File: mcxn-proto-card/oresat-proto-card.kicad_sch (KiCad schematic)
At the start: 0 parts

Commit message: Fully routed MCXN947 proto card, still needs final polish.
Big cleanup of the proto card's OPD, bringing it up to modern standards. Also fixed the v2 backplane connector. Added the MCXN937 processor, and breakouts for the unused pins. Switched to the new debug connector, which will be fun. That's it!
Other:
- title: OreSat M0 Proto Card -> OreSat MCXN Proto Card
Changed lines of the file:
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@@
 	(paper "USLedger")
 	(title_block
-		(title "OreSat M0 Proto Card")
-		(date "2025-06-29")
-		(rev "5.0")
+		(title "OreSat MCXN Proto Card")
+		(date "2025-11-13")
+		(rev "6.0")
 	)
 	(sheet

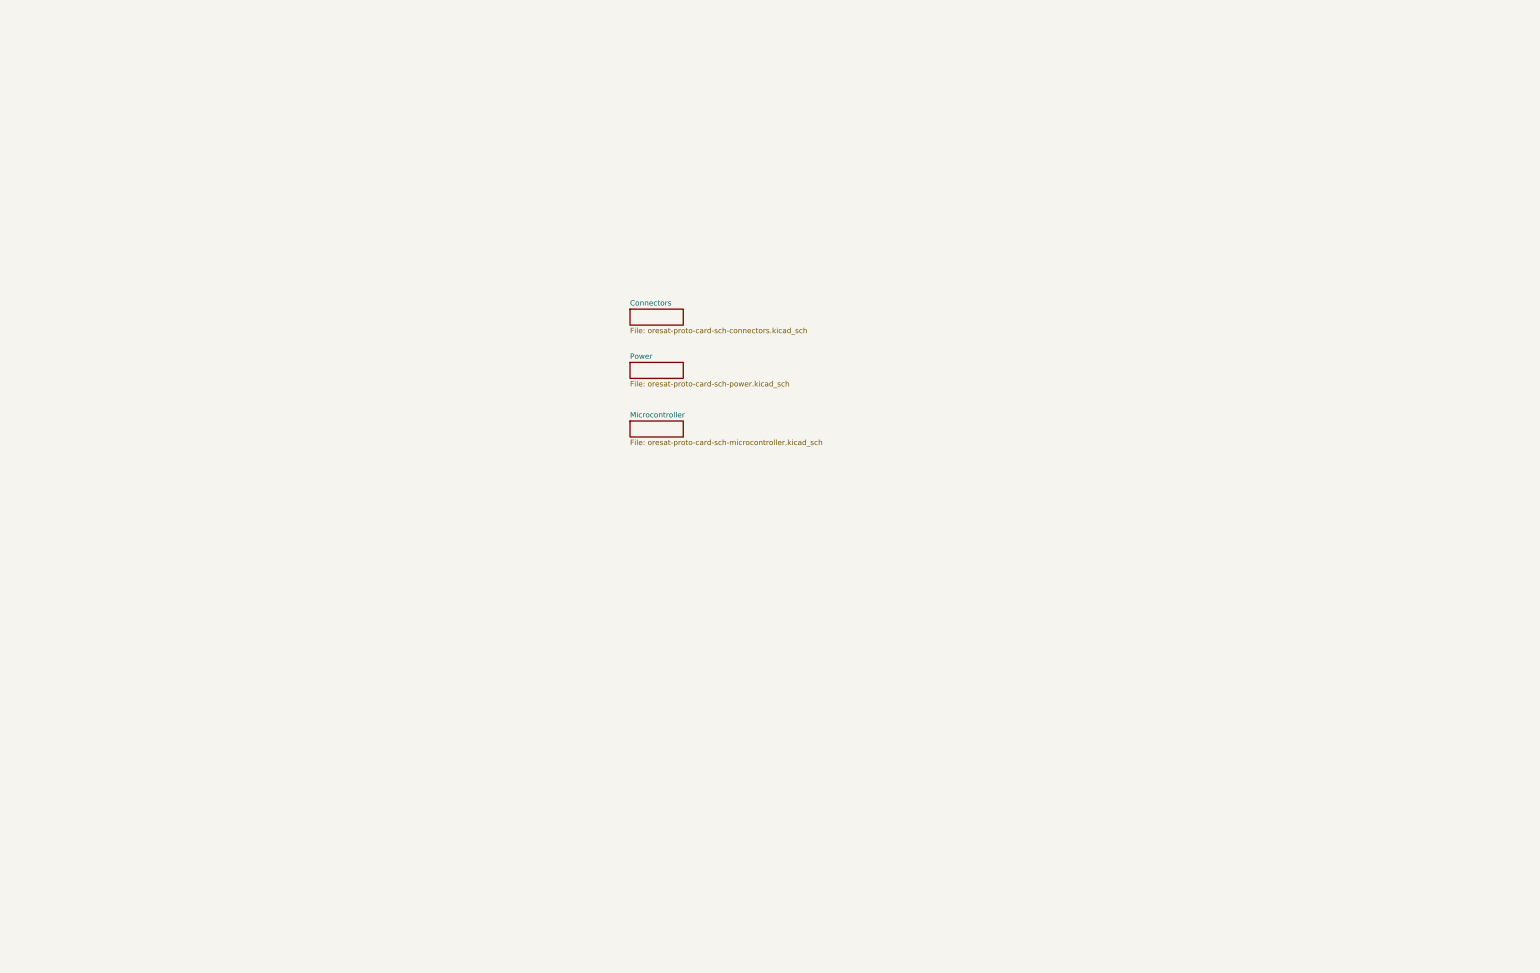
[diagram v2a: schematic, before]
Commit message: Final MCXN protocard cleanup
Made schematic fancy with hierarchical pins, cleaned up schematics a bit, and fixed silk screen a ton. Ready for fab.
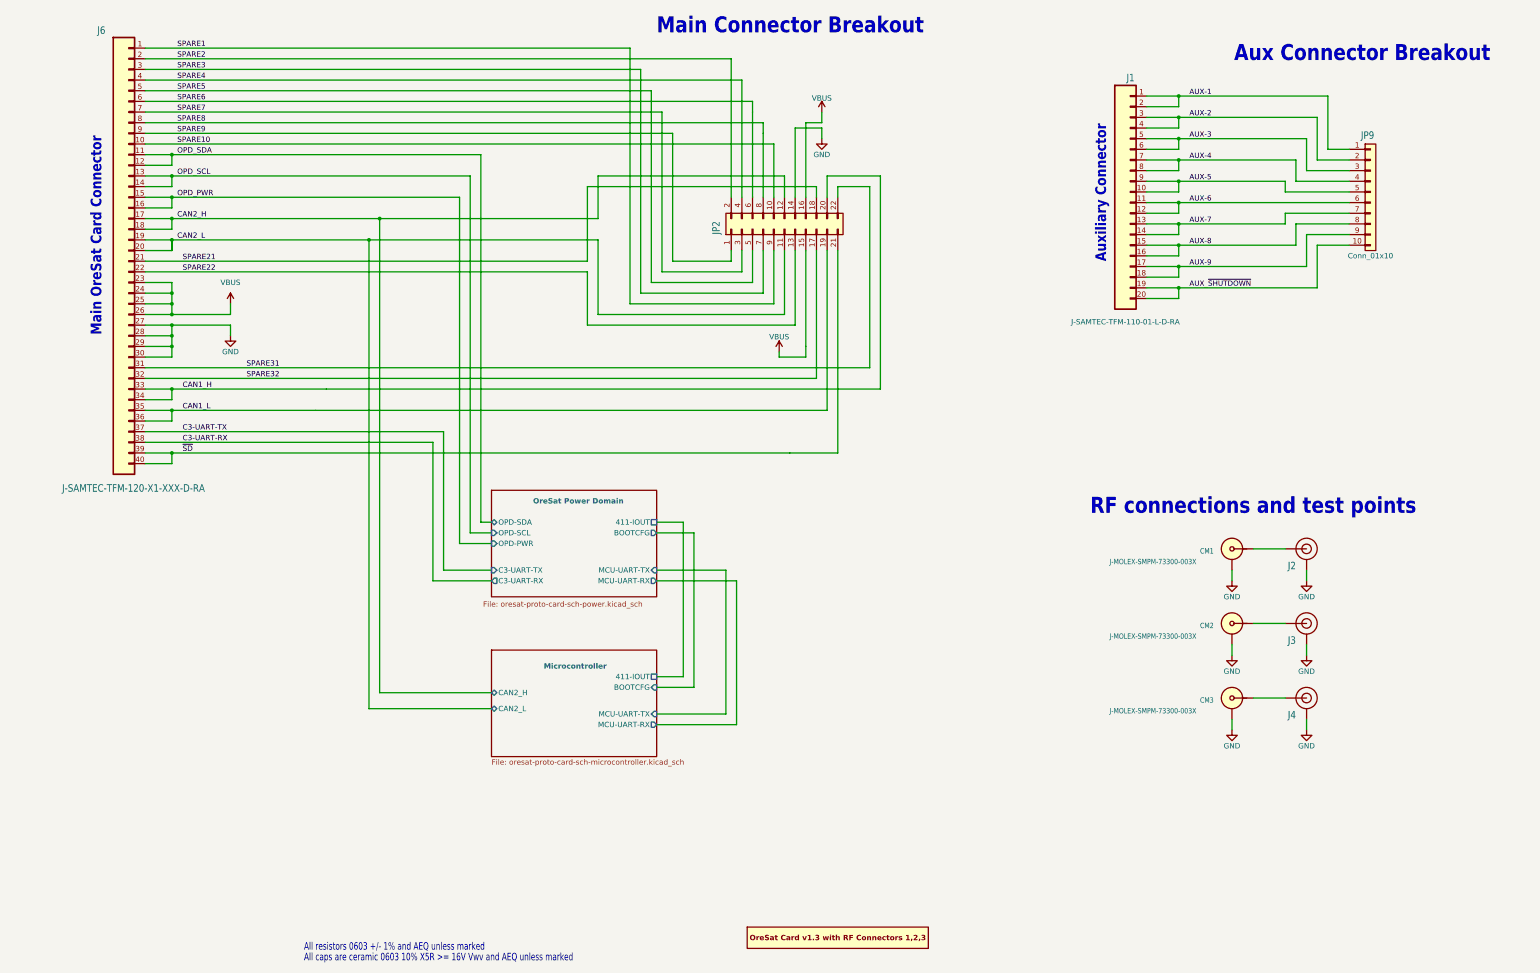
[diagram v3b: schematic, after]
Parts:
- added CM1, CM2, CM3: J-MOLEX-SMPM-73300-003X, oresat-connectors:J-MOLEX-SMPM-073300-002X, symbol oresat-connectors:J-MOLEX-SMPM-73300-002X
- added J1: J-SAMTEC-TFM-110-01-L-D-RA, oresat-connectors:J-SAMTEC-TFM-110-X1-XXX-D-RA, symbol oresat-connectors:J-SAMTEC-TFM-110-01-L-D-RA
- added J2, J3, J4: U.FL, oresat-connectors:J-U.FL, symbol oresat-connectors:U.FL2PIN
- added J6: J-SAMTEC-TFM-120-X1-XXX-D-RA, oresat-connectors:J-SAMTEC-TFM-120-X1-XXX-D-RA, symbol oresat-connectors:J-SAMTEC-TFM-120-01-L-D-RA
- added JP2: PINHD-2X5, Connector_PinHeader_2.54mm:PinHeader_2x11_P2.54mm_Vertical, symbol Connector_Generic:Conn_02x11_Odd_Even
- added JP9: Conn_01x10, Connector_PinHeader_2.54mm:PinHeader_1x10_P2.54mm_Vertical, symbol Connector_Generic:Conn_01x10
- added PCB1: ORESAT-CARD-V1.3-3RF, oresat-pcbs:ORESAT-CARD-V1.3-3RF, symbol oresat-pcbs:ORESAT-CARD-V1.3-3RF
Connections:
- new net: CM2.SIG, J3.FEED (SIGNAL)
- new net: CM1.SIG, J2.FEED (SIGNAL)
- new net: J6.15, J6.16
- new net: CM3.SIG, J4.FEED (SIGNAL)
- new net AUX-1: J1.1, J1.2, JP9.1 (Pin_1)
- new net AUX-2: J1.3, J1.4, JP9.2 (Pin_2)
- new net AUX-3: J1.5, J1.6, JP9.3 (Pin_3)
- new net AUX-4: J1.7, J1.8, JP9.4 (Pin_4)
- new net AUX-5: J1.10, J1.9, JP9.5 (Pin_5)
- new net AUX-6: J1.11, J1.12, JP9.6 (Pin_6)
- new net AUX-7: J1.13, J1.14, JP9.7 (Pin_7)
- new net AUX-8: J1.15, J1.16, JP9.8 (Pin_8)
- new net AUX-9: J1.17, J1.18, JP9.9 (Pin_9)
- new net AUX_~{SHUTDOWN}: J1.19, J1.20, JP9.10 (Pin_10)
- new net C3-UART-RX: J6.38
- new net C3-UART-TX: J6.37
- new net CAN1_H: J6.33, J6.34, JP2.20 (Pin_20)
- new net CAN1_L: J6.35, J6.36, JP2.19 (Pin_19)
- new net CAN2_H: J6.17, J6.18, JP2.12 (Pin_12)
- new net CAN2_L: J6.19, J6.20, JP2.11 (Pin_11)
- new net GND: CM1.SHLD, CM2.SHLD, CM3.SHLD, J2.GND, J3.GND, J4.GND, J6.27, J6.28, J6.29, J6.30, JP2.14 (Pin_14)
- new net OPD_SCL: J6.13, J6.14
- new net OPD_SDA: J6.11, J6.12
- new net SPARE1: J6.1, JP2.9 (Pin_9)
- new net SPARE10: J6.10, JP2.10 (Pin_10)
- new net SPARE2: J6.2, JP2.2 (Pin_2)
- new net SPARE21: J6.21, JP2.18 (Pin_18)
- new net SPARE22: J6.22, JP2.13 (Pin_13)
- new net SPARE3: J6.3, JP2.7 (Pin_7)
- new net SPARE31: J6.31, JP2.22 (Pin_22)
- new net SPARE32: J6.32, JP2.17 (Pin_17)
- new net SPARE4: J6.4, JP2.4 (Pin_4)
- new net SPARE5: J6.5, JP2.5 (Pin_5)
- new net SPARE6: J6.6, JP2.6 (Pin_6)
- new net SPARE7: J6.7, JP2.3 (Pin_3)
- new net SPARE8: J6.8, JP2.8 (Pin_8)
- new net SPARE9: J6.9, JP2.1 (Pin_1)
- new net VBUS: J6.23, J6.24, J6.25, J6.26, JP2.15 (Pin_15), JP2.16 (Pin_16)
- new net ~{SD}: J6.39, J6.40, JP2.21 (Pin_21)
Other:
- sheet Power renamed OreSat Power Domain
- removed sheet Connectors
- sheet Microcontroller ports: added 411-IOUT, BOOTCFG, CAN2_H, CAN2_L, MCU-UART-RX, MCU-UART-TX; removed none
- sheet OreSat Power Domain ports: added 411-IOUT, BOOTCFG, C3-UART-RX, C3-UART-TX, MCU-UART-RX, MCU-UART-TX, OPD-PWR, OPD-SCL, OPD-SDA; removed none
- note added: "All caps are ceramic 0603 10% X5R >= 16V Vwv and AEQ unless marked"
- note added: "All resistors 0603 +/- 1% and AEQ unless marked"
- note added: "Aux Connector Breakout"
- note added: "Auxiliary Connector"
- note added: "Main Connector Breakout"
- note added: "Main OreSat Card Connector"
- note added: "RF connections and test points"
- company: (none) -> Portland State Aerospace Society

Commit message: BOM fixed; schematic polish (no change to PCB v6.0)
Fixed BOM, and synced with OreSat BOMs Google Sheet. Figured out large capacitor (> 4.7u) voltages and package issues, which are many. Set MCXN pin names to the right selection if possible.
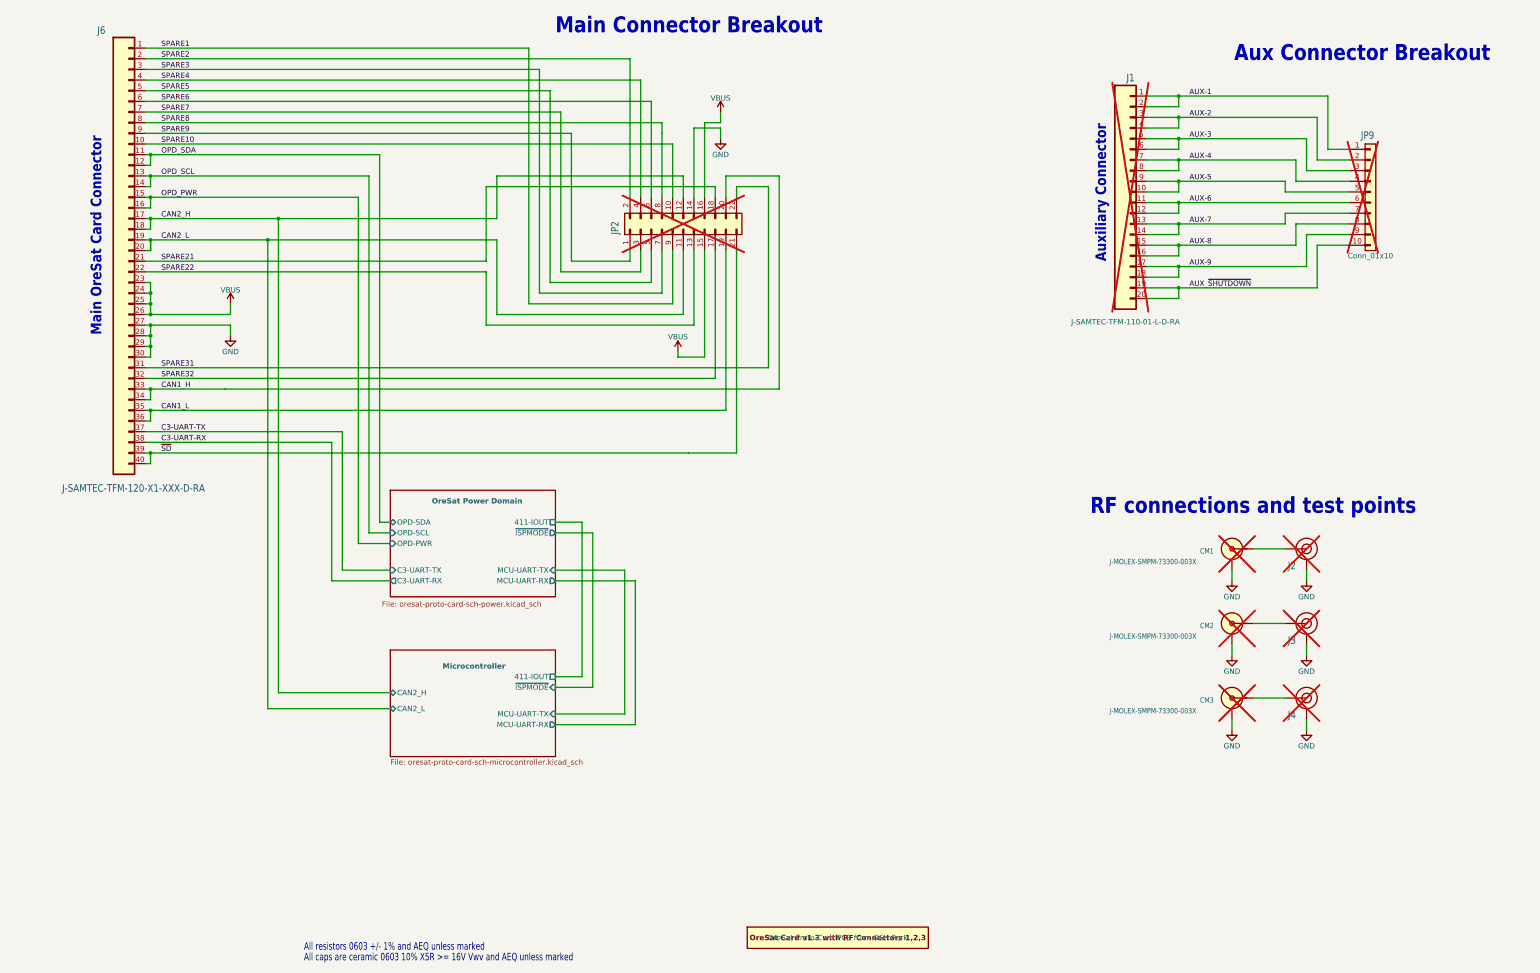
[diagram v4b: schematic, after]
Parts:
- CM1, CM2, CM3, J2, J3, J4, JP9: DIS Digi-Key -> DigiKey; now not fitted
- J1: DIS Digikey -> DigiKey; now not fitted
- J6: DIS Digi-Key -> DigiKey
- JP2: DIS (none) -> DigiKey; now not fitted
- PCB1: DIS (none) -> NA; DPN (none) -> NA; MFR (none) -> OSH Park; MPN (none) -> oresat-proto-card-v6.0-2025-12-28
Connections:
- net OPD_PWR: now reaches J6.15, J6.16
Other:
- sheet Microcontroller ports: added ~{ISPMODE}; removed BOOTCFG
- sheet OreSat Power Domain ports: added ~{ISPMODE}; removed BOOTCFG
